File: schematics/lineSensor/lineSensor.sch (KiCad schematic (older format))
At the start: 27 parts, among them P1 CONN_01X01, P2 CONN_01X01, P3 CONN_01X01, P4 CONN_01X01, P5 CONN_01X01, P6 CONN_01X01, P7 CONN_01X01

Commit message: Cleanup repository
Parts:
- R1, R3, R5, R7, R9: value R -> 150
- R10, R2, R4, R6, R8: value R -> 510k
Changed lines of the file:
@@
 P 4600 4200
 F 0 "R1" V 4680 4200 50  0000 C CNN
-F 1 "R" V 4600 4200 50  0000 C CNN
+F 1 "150" V 4600 4200 50  0000 C CNN
 F 2 "w_pth_resistors:rc05_vert" V 4530 4200 50  0001 C CNN
 F 3 "" H 4600 4200 50  0000 C CNN
@@
 P 4850 4200
 F 0 "R2" V 4930 4200 50  0000 C CNN
-F 1 "R" V 4850 4200 50  0000 C CNN
+F 1 "510k" V 4850 4200 50  0000 C CNN
 F 2 "w_pth_resistors:rc05_vert" V 4780 4200 50  0001 C CNN
 F 3 "" H 4850 4200 50  0000 C CNN
@@
 P 5200 4200
 F 0 "R3" V 5280 4200 50  0000 C CNN
-F 1 "R" V 5200 4200 50  0000 C CNN
+F 1 "150" V 5200 4200 50  0000 C CNN
 F 2 "w_pth_resistors:rc05_vert" V 5130 4200 50  0001 C CNN
 F 3 "" H 5200 4200 50  0000 C CNN
@@
 P 5450 4200
 F 0 "R4" V 5530 4200 50  0000 C CNN
-F 1 "R" V 5450 4200 50  0000 C CNN
+F 1 "510k" V 5450 4200 50  0000 C CNN
 F 2 "w_pth_resistors:rc05_vert" V 5380 4200 50  0001 C CNN
 F 3 "" H 5450 4200 50  0000 C CNN
@@
 P 5800 4200
 F 0 "R5" V 5880 4200 50  0000 C CNN
-F 1 "R" V 5800 4200 50  0000 C CNN
+F 1 "150" V 5800 4200 50  0000 C CNN
 F 2 "w_pth_resistors:rc05_vert" V 5730 4200 50  0001 C CNN
 F 3 "" H 5800 4200 50  0000 C CNN
@@
 P 6050 4200
 F 0 "R6" V 6130 4200 50  0000 C CNN
-F 1 "R" V 6050 4200 50  0000 C CNN
+F 1 "510k" V 6050 4200 50  0000 C CNN
 F 2 "w_pth_resistors:rc05_vert" V 5980 4200 50  0001 C CNN
 F 3 "" H 6050 4200 50  0000 C CNN
@@
 P 6400 4200
 F 0 "R7" V 6480 4200 50  0000 C CNN
-F 1 "R" V 6400 4200 50  0000 C CNN
+F 1 "150" V 6400 4200 50  0000 C CNN
 F 2 "Resistors_ThroughHole:Resistor_Horizontal_RM15mm" V 6330 4200 50  0001 C CNN
 F 3 "" H 6400 4200 50  0000 C CNN
@@
 P 6650 4200
 F 0 "R8" V 6730 4200 50  0000 C CNN
-F 1 "R" V 6650 4200 50  0000 C CNN
+F 1 "510k" V 6650 4200 50  0000 C CNN
 F 2 "Resistors_ThroughHole:Resistor_Horizontal_RM15mm" V 6580 4200 50  0001 C CNN
 F 3 "" H 6650 4200 50  0000 C CNN
@@
 P 7000 4200
 F 0 "R9" V 7080 4200 50  0000 C CNN
-F 1 "R" V 7000 4200 50  0000 C CNN
+F 1 "150" V 7000 4200 50  0000 C CNN
 F 2 "Resistors_ThroughHole:Resistor_Horizontal_RM15mm" V 6930 4200 50  0001 C CNN
 F 3 "" H 7000 4200 50  0000 C CNN
@@
 P 7250 4200
 F 0 "R10" V 7330 4200 50  0000 C CNN
-F 1 "R" V 7250 4200 50  0000 C CNN
+F 1 "510k" V 7250 4200 50  0000 C CNN
 F 2 "Resistors_ThroughHole:Resistor_Horizontal_RM15mm" V 7180 4200 50  0001 C CNN
 F 3 "" H 7250 4200 50  0000 C CNN

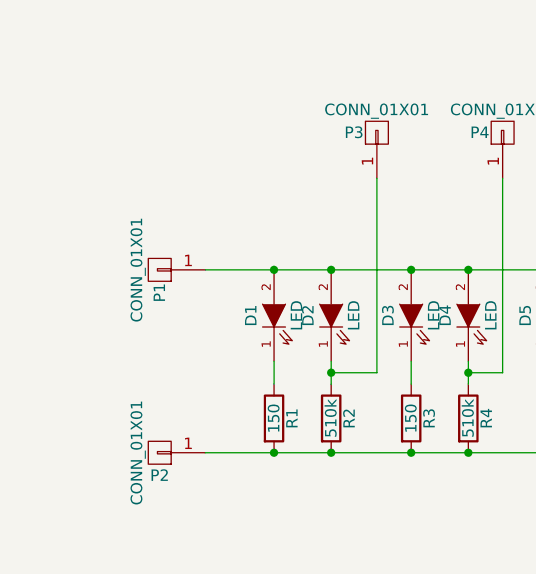
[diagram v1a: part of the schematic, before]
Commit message: Update schematics for whiskers
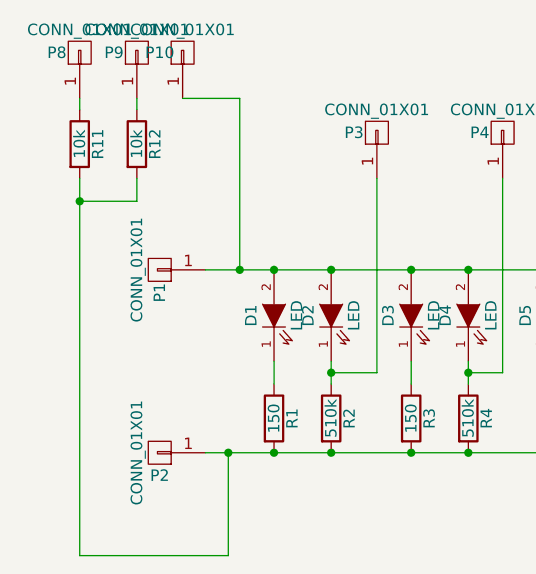
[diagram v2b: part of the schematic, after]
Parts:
- added P10, P8, P9: CONN_01X01, Pin_Headers:Pin_Header_Straight_1x01, symbol CONN_01X01
- added R11, R12: 10k, w_pth_resistors:rc05_vert, symbol R
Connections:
- net at D1.2 (A), D10.2 (A), D2.2 (A)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: now also P10.1 (P1)
- net at P2.1 (P1), R1.2, R10.2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: now also R11.2, R12.2
- new net: P9.1 (P1), R12.1
- new net: P8.1 (P1), R11.1
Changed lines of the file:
@@
 	7400 4000 7250 4000
 Connection ~ 7250 4000
+$Comp
+L CONN_01X01 P10
+U 1 1 5724A1DF
+P 4200 2600
+F 0 "P10" V 4200 2700 50  0000 C CNN
+F 1 "CONN_01X01" V 4300 2600 50  0000 C CNN
+F 2 "Pin_Headers:Pin_Header_Straight_1x01" H 4200 2600 50  0001 C CNN
+F 3 "" H 4200 2600 50  0000 C CNN
+	1    4200 2600
+	0    -1   -1   0
+$EndComp
+$Comp
+L CONN_01X01 P9
+U 1 1 5724A2A5
+P 4000 2600
+F 0 "P9" V 4000 2700 50  0000 C CNN
+F 1 "CONN_01X01" V 4100 2600 50  0000 C CNN
+F 2 "Pin_Headers:Pin_Header_Straight_1x01" H 4000 2600 50  0001 C CNN
+F 3 "" H 4000 2600 50  0000 C CNN
+	1    4000 2600
+	0    -1   -1   0
+$EndComp
+$Comp
+L CONN_01X01 P8
+U 1 1 5724A372
+P 3750 2600
+F 0 "P8" V 3750 2700 50  0000 C CNN
+F 1 "CONN_01X01" V 3850 2600 50  0000 C CNN
+F 2 "Pin_Headers:Pin_Header_Straight_1x01" H 3750 2600 50  0001 C CNN
+F 3 "" H 3750 2600 50  0000 C CNN
+	1    3750 2600
+	0    -1   -1   0
+$EndComp
+Wire Wire Line
+	4450 3550 4450 2800
+Wire Wire Line
+	4450 2800 4200 2800
+Connection ~ 4450 3550
+$Comp
+L R R11
+U 1 1 5724A48E
+P 3750 3000
+F 0 "R11" V 3830 3000 50  0000 C CNN
+F 1 "10k" V 3750 3000 50  0000 C CNN
+F 2 "w_pth_resistors:rc05_vert" V 3680 3000 50  0001 C CNN
+F 3 "" H 3750 3000 50  0000 C CNN
+	1    3750 3000
+	1    0    0    -1
+$EndComp
+$Comp
+L R R12
+U 1 1 5724A596
+P 4000 3000
+F 0 "R12" V 4080 3000 50  0000 C CNN
+F 1 "10k" V 4000 3000 50  0000 C CNN
+F 2 "w_pth_resistors:rc05_vert" V 3930 3000 50  0001 C CNN
+F 3 "" H 4000 3000 50  0000 C CNN
+	1    4000 3000
+	1    0    0    -1
+$EndComp
+Wire Wire Line
+	3750 2850 3750 2800
+Wire Wire Line
+	4000 2850 4000 2800
+Wire Wire Line
+	4000 3150 4000 3250
+Wire Wire Line
+	4000 3250 3750 3250
+Wire Wire Line
+	3750 3150 3750 4800
+Wire Wire Line
+	3750 4800 4400 4800
+Wire Wire Line
+	4400 4800 4400 4350
+Connection ~ 4400 4350
+Connection ~ 3750 3250
 $EndSCHEMATC

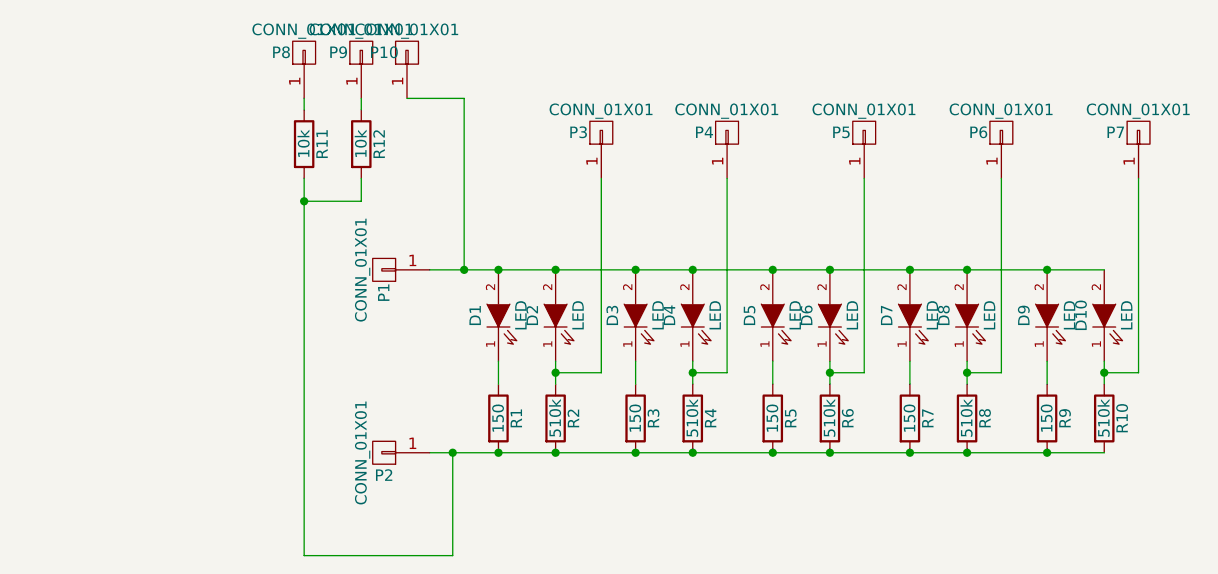
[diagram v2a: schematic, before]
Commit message: Update lineSensor board for sonar power
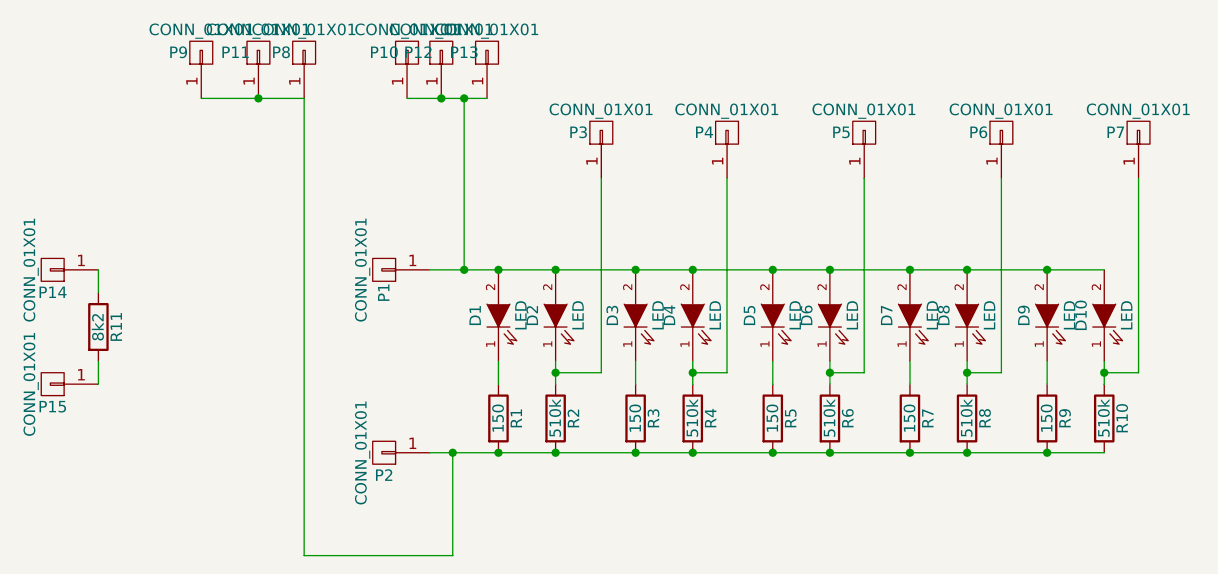
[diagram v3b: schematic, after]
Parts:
- removed R12: 10k, w_pth_resistors:rc05_vert, symbol R
- added P11, P12, P13, P14, P15: CONN_01X01, Pin_Headers:Pin_Header_Straight_1x01, symbol CONN_01X01
- R11: value 10k -> 8k2
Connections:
- net at D1.2 (A), D10.2 (A), D2.2 (A)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: now also P12.1 (P1), P13.1 (P1)
- net at P2.1 (P1), R1.2, R10.2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: now also P8.1 (P1), P9.1 (P1), P11.1 (P1); no longer R11.2
- net at R11.1: now also P14.1 (P1); no longer P8.1 (P1)
- new net: P15.1 (P1), R11.2
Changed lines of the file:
@@
 	-1   0    0    1
+$EndComp
+$Comp
+L CONN_01X01 P4
+U 1 1 56E975AA
+P 5600 2950
+F 0 "P4" V 5600 3050 50  0000 C CNN
+F 1 "CONN_01X01" V 5700 2950 50  0000 C CNN
+F 2 "Pin_Headers:Pin_Header_Straight_1x01" H 5600 2950 50  0001 C CNN
+F 3 "" H 5600 2950 50  0000 C CNN
+	1    5600 2950
+	0    -1   -1   0
+$EndComp
+$Comp
+L CONN_01X01 P3
+U 1 1 56E975AB
+P 5050 2950
+F 0 "P3" V 5050 3050 50  0000 C CNN
+F 1 "CONN_01X01" V 5150 2950 50  0000 C CNN
+F 2 "Pin_Headers:Pin_Header_Straight_1x01" H 5050 2950 50  0001 C CNN
+F 3 "" H 5050 2950 50  0000 C CNN
+	1    5050 2950
+	0    -1   -1   0
+$EndComp
+$Comp
+L CONN_01X01 P5
+U 1 1 56E975AC
+P 6200 2950
+F 0 "P5" V 6200 3050 50  0000 C CNN
+F 1 "CONN_01X01" V 6300 2950 50  0000 C CNN
+F 2 "Pin_Headers:Pin_Header_Straight_1x01" H 6200 2950 50  0001 C CNN
+F 3 "" H 6200 2950 50  0000 C CNN
+	1    6200 2950
+	0    -1   -1   0
+$EndComp
+$Comp
+L CONN_01X01 P6
+U 1 1 56E975AD
+P 6800 2950
+F 0 "P6" V 6800 3050 50  0000 C CNN
+F 1 "CONN_01X01" V 6900 2950 50  0000 C CNN
+F 2 "Pin_Headers:Pin_Header_Straight_1x01" H 6800 2950 50  0001 C CNN
+F 3 "" H 6800 2950 50  0000 C CNN
+	1    6800 2950
+	0    -1   -1   0
+$EndComp
+$Comp
+L CONN_01X01 P7
+U 1 1 56E975AE
+P 7400 2950
+F 0 "P7" V 7400 3050 50  0000 C CNN
+F 1 "CONN_01X01" V 7500 2950 50  0000 C CNN
+F 2 "Pin_Headers:Pin_Header_Straight_1x01" H 7400 2950 50  0001 C CNN
+F 3 "" H 7400 2950 50  0000 C CNN
+	1    7400 2950
+	0    -1   -1   0
+$EndComp
+$Comp
+L CONN_01X01 P10
+U 1 1 5724A1DF
+P 4200 2600
+F 0 "P10" V 4200 2700 50  0000 C CNN
+F 1 "CONN_01X01" V 4300 2600 50  0000 C CNN
+F 2 "Pin_Headers:Pin_Header_Straight_1x01" H 4200 2600 50  0001 C CNN
+F 3 "" H 4200 2600 50  0000 C CNN
+	1    4200 2600
+	0    -1   -1   0
+$EndComp
+$Comp
+L CONN_01X01 P8
+U 1 1 5724A372
+P 3750 2600
+F 0 "P8" V 3750 2700 50  0000 C CNN
+F 1 "CONN_01X01" V 3850 2600 50  0000 C CNN
+F 2 "Pin_Headers:Pin_Header_Straight_1x01" H 3750 2600 50  0001 C CNN
+F 3 "" H 3750 2600 50  0000 C CNN
+	1    3750 2600
+	0    -1   -1   0
+$EndComp
+$Comp
+L CONN_01X01 P11
+U 1 1 5728B633
+P 3550 2600
+F 0 "P11" V 3550 2700 50  0000 C CNN
+F 1 "CONN_01X01" V 3650 2600 50  0000 C CNN
+F 2 "Pin_Headers:Pin_Header_Straight_1x01" H 3550 2600 50  0001 C CNN
+F 3 "" H 3550 2600 50  0000 C CNN
+	1    3550 2600
+	0    -1   -1   0
+$EndComp
+$Comp
+L CONN_01X01 P9
+U 1 1 5728B6A1
+P 3300 2600
+F 0 "P9" V 3300 2700 50  0000 C CNN
+F 1 "CONN_01X01" V 3400 2600 50  0000 C CNN
+F 2 "Pin_Headers:Pin_Header_Straight_1x01" H 3300 2600 50  0001 C CNN
+F 3 "" H 3300 2600 50  0000 C CNN
+	1    3300 2600
+	0    -1   -1   0
+$EndComp
+$Comp
+L CONN_01X01 P12
+U 1 1 5728B718
+P 4350 2600
+F 0 "P12" V 4350 2700 50  0000 C CNN
+F 1 "CONN_01X01" V 4450 2600 50  0000 C CNN
+F 2 "Pin_Headers:Pin_Header_Straight_1x01" H 4350 2600 50  0001 C CNN
+F 3 "" H 4350 2600 50  0000 C CNN
+	1    4350 2600
+	0    -1   -1   0
+$EndComp
+$Comp
+L CONN_01X01 P13
+U 1 1 5728B78E
+P 4550 2600
+F 0 "P13" V 4550 2700 50  0000 C CNN
+F 1 "CONN_01X01" V 4650 2600 50  0000 C CNN
+F 2 "Pin_Headers:Pin_Header_Straight_1x01" H 4550 2600 50  0001 C CNN
+F 3 "" H 4550 2600 50  0000 C CNN
+	1    4550 2600
+	0    -1   -1   0
 $EndComp
 Wire Wire Line
@@
 Connection ~ 4850 4350
 Connection ~ 4600 4350
-$Comp
-L CONN_01X01 P4
-U 1 1 56E975AA
-P 5600 2950
-F 0 "P4" V 5600 3050 50  0000 C CNN
-F 1 "CONN_01X01" V 5700 2950 50  0000 C CNN
-F 2 "Pin_Headers:Pin_Header_Straight_1x01" H 5600 2950 50  0001 C CNN
-F 3 "" H 5600 2950 50  0000 C CNN
-	1    5600 2950
-	0    -1   -1   0
-$EndComp
-$Comp
-L CONN_01X01 P3
-U 1 1 56E975AB
-P 5050 2950
-F 0 "P3" V 5050 3050 50  0000 C CNN
-F 1 "CONN_01X01" V 5150 2950 50  0000 C CNN
-F 2 "Pin_Headers:Pin_Header_Straight_1x01" H 5050 2950 50  0001 C CNN
-F 3 "" H 5050 2950 50  0000 C CNN
-	1    5050 2950
-	0    -1   -1   0
-$EndComp
-$Comp
-L CONN_01X01 P5
-U 1 1 56E975AC
-P 6200 2950
-F 0 "P5" V 6200 3050 50  0000 C CNN
-F 1 "CONN_01X01" V 6300 2950 50  0000 C CNN
-F 2 "Pin_Headers:Pin_Header_Straight_1x01" H 6200 2950 50  0001 C CNN
-F 3 "" H 6200 2950 50  0000 C CNN
-	1    6200 2950
-	0    -1   -1   0
-$EndComp
-$Comp
-L CONN_01X01 P6
-U 1 1 56E975AD
-P 6800 2950
-F 0 "P6" V 6800 3050 50  0000 C CNN
-F 1 "CONN_01X01" V 6900 2950 50  0000 C CNN
-F 2 "Pin_Headers:Pin_Header_Straight_1x01" H 6800 2950 50  0001 C CNN
-F 3 "" H 6800 2950 50  0000 C CNN
-	1    6800 2950
-	0    -1   -1   0
-$EndComp
-$Comp
-L CONN_01X01 P7
-U 1 1 56E975AE
-P 7400 2950
-F 0 "P7" V 7400 3050 50  0000 C CNN
-F 1 "CONN_01X01" V 7500 2950 50  0000 C CNN
-F 2 "Pin_Headers:Pin_Header_Straight_1x01" H 7400 2950 50  0001 C CNN
-F 3 "" H 7400 2950 50  0000 C CNN
-	1    7400 2950
-	0    -1   -1   0
-$EndComp
 Wire Wire Line
 	4600 3950 4600 4050
@@
 	7400 4000 7250 4000
 Connection ~ 7250 4000
-$Comp
-L CONN_01X01 P10
-U 1 1 5724A1DF
-P 4200 2600
-F 0 "P10" V 4200 2700 50  0000 C CNN
-F 1 "CONN_01X01" V 4300 2600 50  0000 C CNN
-F 2 "Pin_Headers:Pin_Header_Straight_1x01" H 4200 2600 50  0001 C CNN
-F 3 "" H 4200 2600 50  0000 C CNN
-	1    4200 2600
-	0    -1   -1   0
-$EndComp
-$Comp
-L CONN_01X01 P9
-U 1 1 5724A2A5
-P 4000 2600
-F 0 "P9" V 4000 2700 50  0000 C CNN
-F 1 "CONN_01X01" V 4100 2600 50  0000 C CNN
-F 2 "Pin_Headers:Pin_Header_Straight_1x01" H 4000 2600 50  0001 C CNN
-F 3 "" H 4000 2600 50  0000 C CNN
-	1    4000 2600
-	0    -1   -1   0
-$EndComp
-$Comp
-L CONN_01X01 P8
-U 1 1 5724A372
-P 3750 2600
-F 0 "P8" V 3750 2700 50  0000 C CNN
-F 1 "CONN_01X01" V 3850 2600 50  0000 C CNN
-F 2 "Pin_Headers:Pin_Header_Straight_1x01" H 3750 2600 50  0001 C CNN
-F 3 "" H 3750 2600 50  0000 C CNN
-	1    3750 2600
-	0    -1   -1   0
-$EndComp
 Wire Wire Line
 	4450 3550 4450 2800
-Wire Wire Line
-	4450 2800 4200 2800
 Connection ~ 4450 3550
-$Comp
-L R R11
-U 1 1 5724A48E
-P 3750 3000
-F 0 "R11" V 3830 3000 50  0000 C CNN
-F 1 "10k" V 3750 3000 50  0000 C CNN
-F 2 "w_pth_resistors:rc05_vert" V 3680 3000 50  0001 C CNN
-F 3 "" H 3750 3000 50  0000 C CNN
-	1    3750 3000
-	1    0    0    -1
-$EndComp
-$Comp
-L R R12
-U 1 1 5724A596
-P 4000 3000
-F 0 "R12" V 4080 3000 50  0000 C CNN
-F 1 "10k" V 4000 3000 50  0000 C CNN
-F 2 "w_pth_resistors:rc05_vert" V 3930 3000 50  0001 C CNN
-F 3 "" H 4000 3000 50  0000 C CNN
-	1    4000 3000
-	1    0    0    -1
-$EndComp
-Wire Wire Line
-	3750 2850 3750 2800
-Wire Wire Line
-	4000 2850 4000 2800
-Wire Wire Line
-	4000 3150 4000 3250
-Wire Wire Line
-	4000 3250 3750 3250
-Wire Wire Line
-	3750 3150 3750 4800
+Wire Wire Line
+	3750 2800 3750 4800
 Wire Wire Line
 	3750 4800 4400 4800
@@
 	4400 4800 4400 4350
 Connection ~ 4400 4350
-Connection ~ 3750 3250
+Connection ~ 4450 2800
+Wire Wire Line
+	4200 2800 4550 2800
+Connection ~ 4350 2800
+Wire Wire Line
+	3300 2800 3750 2800
+Connection ~ 3550 2800
+$Comp
+L CONN_01X01 P15
+U 1 1 5728B887
+P 2650 4050
+F 0 "P15" H 2650 4150 50  0000 C CNN
+F 1 "CONN_01X01" V 2750 4050 50  0000 C CNN
+F 2 "Pin_Headers:Pin_Header_Straight_1x01" H 2650 4050 50  0001 C CNN
+F 3 "" H 2650 4050 50  0000 C CNN
+	1    2650 4050
+	-1   0    0    1
+$EndComp
+$Comp
+L R R11
+U 1 1 5728B949
+P 2850 3800
+F 0 "R11" V 2930 3800 50  0000 C CNN
+F 1 "8k2" V 2850 3800 50  0000 C CNN
+F 2 "w_pth_resistors:rc05_vert" V 2780 3800 50  0001 C CNN
+F 3 "" H 2850 3800 50  0000 C CNN
+	1    2850 3800
+	1    0    0    -1
+$EndComp
+$Comp
+L CONN_01X01 P14
+U 1 1 5728BAAE
+P 2650 3550
+F 0 "P14" H 2650 3650 50  0000 C CNN
+F 1 "CONN_01X01" V 2750 3550 50  0000 C CNN
+F 2 "Pin_Headers:Pin_Header_Straight_1x01" H 2650 3550 50  0001 C CNN
+F 3 "" H 2650 3550 50  0000 C CNN
+	1    2650 3550
+	-1   0    0    1
+$EndComp
+Wire Wire Line
+	2850 3650 2850 3550
+Wire Wire Line
+	2850 3950 2850 4050
 $EndSCHEMATC
